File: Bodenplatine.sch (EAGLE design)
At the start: 113 parts, among them K1 RY612012, K2 RY612012, K3 RY612012, K4 RY612012, K5 RY612012, K6 RY612012, K7 RY612012, K8 RY612012, K9 RY612012, Q1 BC846BLT1SMD, Q2 BC846BLT1SMD, Q3 BC846BLT1SMD, Q4 BC846BLT1SMD, Q5 BC846BLT1SMD, Q6 BC846BLT1SMD, Q7 BC846BLT1SMD, Q8 BC846BLT1SMD, Q9 BC846BLT1SMD, X1 SPRINGCON_AST125_5X2, X10 SPRINGCON_AST125_3X2, X11 SPRINGCON_AST125_4X2, X12 SPRINGCON_AST125_4X2, X13 SPRINGCON_AST125_5X2, X14 236-403, X15 236-402, X2 SPRINGCON_AST125_5X2, X3 SPRINGCON_AST125_5X2, X4 SPRINGCON_AST125_5X2, X5 SPRINGCON_AST125_5X2, X6 SPRINGCON_AST125_5X2, X7 SPRINGCON_AST125_5X2, X8 SPRINGCON_AST125_5X2, X9 SPRINGCON_AST125_5X2

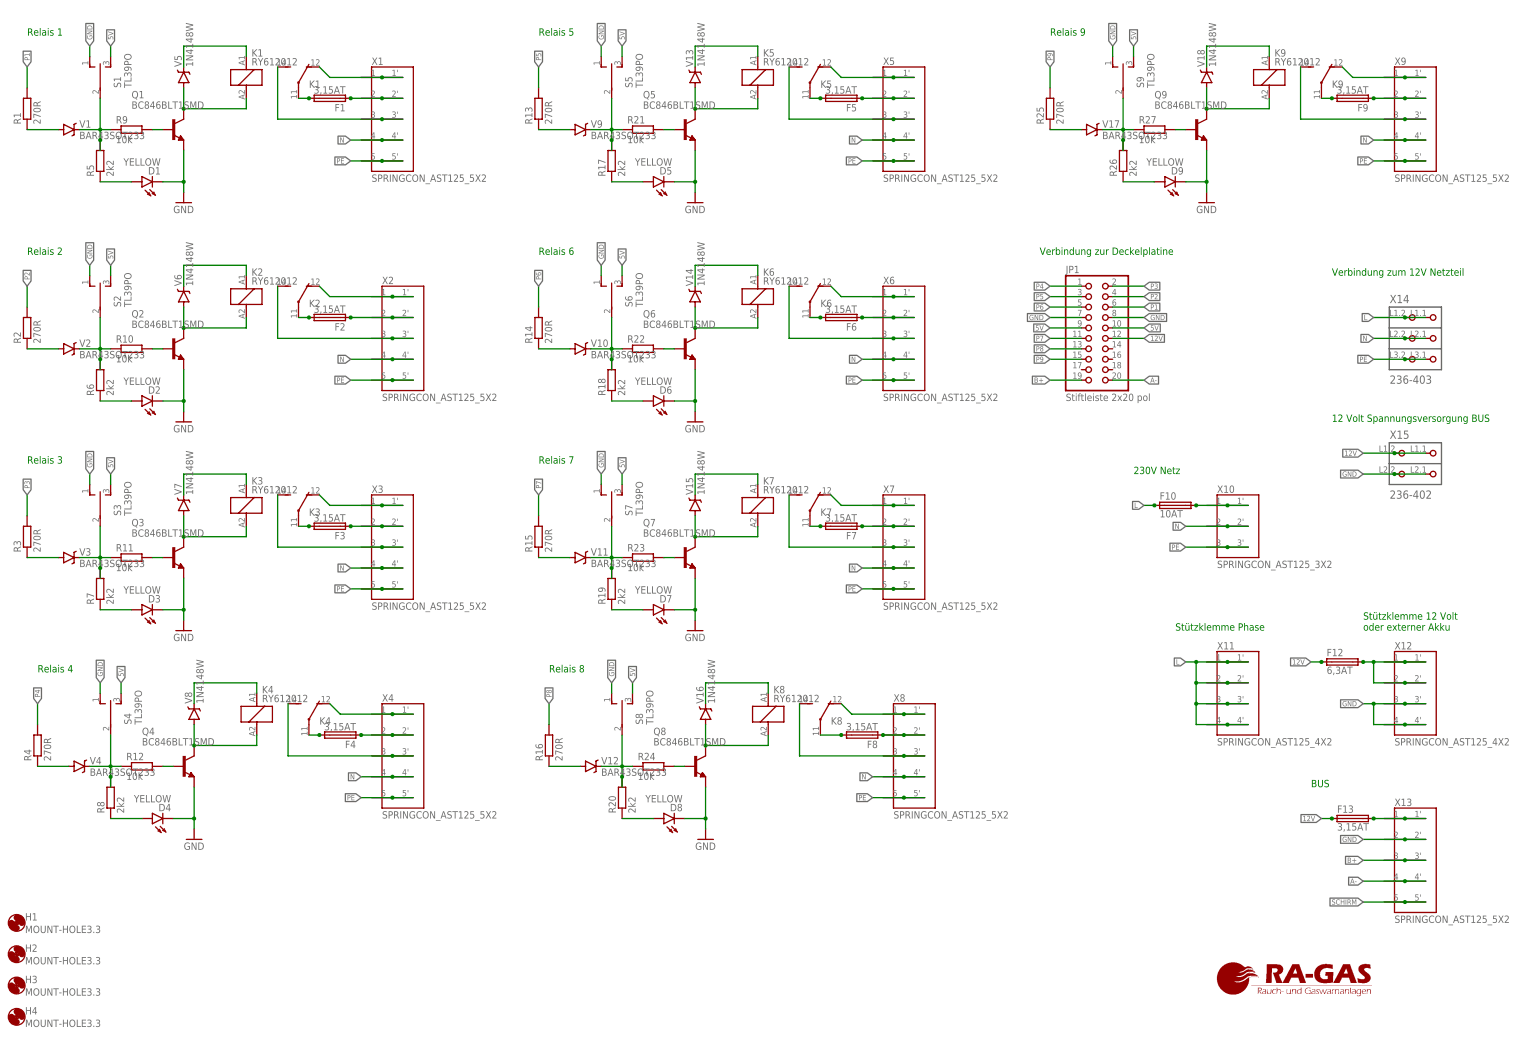
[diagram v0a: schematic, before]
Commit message: Fix 12V Spannungsversorgung vergessen ><
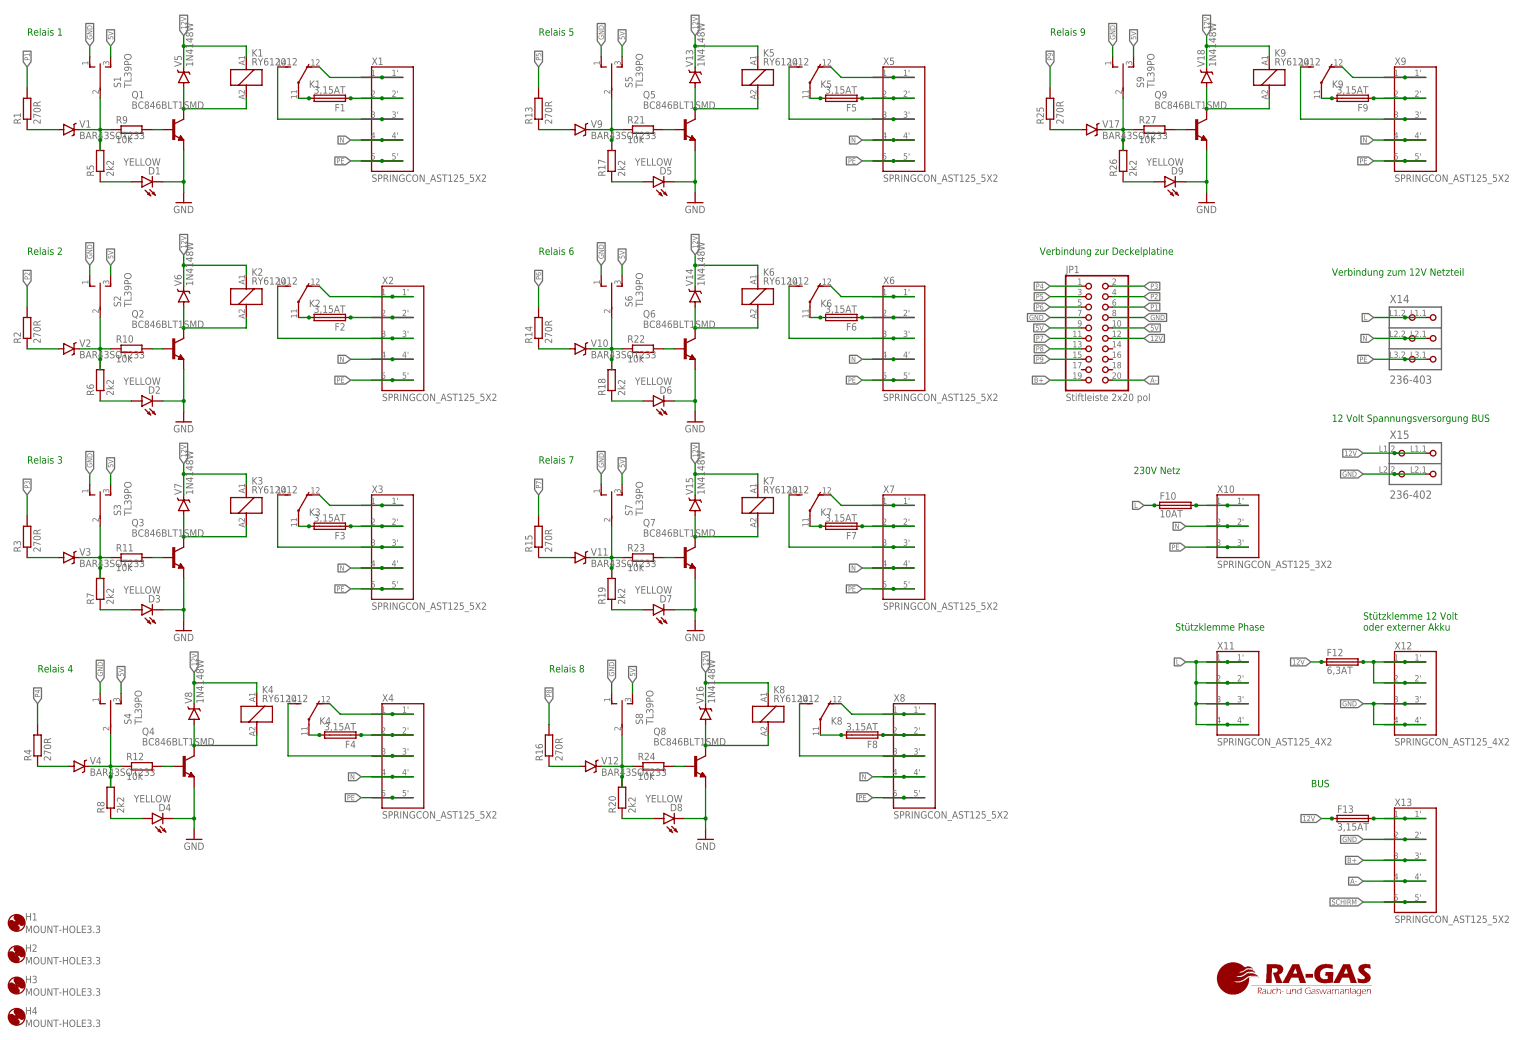
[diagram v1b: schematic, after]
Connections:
- removed net N$11: K21.1, V6.C
- removed net N$17: K31.1, V7.C
- removed net N$27: K41.1, V8.C
- removed net N$37: K51.1, V13.C
- removed net N$47: K61.1, V14.C
- removed net N$57: K71.1, V15.C
- removed net N$67: K81.1, V16.C
- removed net N$77: K91.1, V18.C
- removed net N$87: K11.1, V5.C
- net 12V: now also K11.1, K21.1, K31.1, K41.1, K51.1, K61.1, K71.1, K81.1, K91.1, V13.C, V14.C, V15.C, V16.C, V18.C, V5.C, V6.C, V7.C, V8.C
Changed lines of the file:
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@@
 <attribute name="AUTHOR" value="Stefan Müller"/>
 <attribute name="PROJEKTNAME" value="xMZ-Mod-Touch-Bodenplatine"/>
-<attribute name="VERSION" value="0.0.1"/>
+<attribute name="VERSION" value="0.9.2"/>
 </attributes>
 <variantdefs>
@@
 </segment>
 </net>
-<net name="N$11" class="0">
-<segment>
-<wire x1="50.8" y1="187.96" x2="50.8" y2="193.04" width="0.1524" layer="91"/>
-<pinref part="V6" gate="G$1" pin="C"/>
-<pinref part="K2" gate="1" pin="1"/>
-<wire x1="66.04" y1="190.5" x2="66.04" y2="193.04" width="0.1524" layer="91"/>
-<wire x1="66.04" y1="193.04" x2="50.8" y2="193.04" width="0.1524" layer="91"/>
-</segment>
-</net>
 <net name="N$5" class="0">
 <segment>
@@
 </segment>
 </net>
-<net name="N$17" class="0">
-<segment>
-<wire x1="50.8" y1="137.16" x2="50.8" y2="142.24" width="0.1524" layer="91"/>
-<wire x1="66.04" y1="142.24" x2="50.8" y2="142.24" width="0.1524" layer="91"/>
-<pinref part="V7" gate="G$1" pin="C"/>
-<pinref part="K3" gate="1" pin="1"/>
-<wire x1="66.04" y1="139.7" x2="66.04" y2="142.24" width="0.1524" layer="91"/>
-</segment>
-</net>
 <net name="N$18" class="0">
 <segment>
@@
 </segment>
 </net>
-<net name="N$27" class="0">
-<segment>
-<wire x1="53.34" y1="86.36" x2="53.34" y2="91.44" width="0.1524" layer="91"/>
-<wire x1="68.58" y1="91.44" x2="53.34" y2="91.44" width="0.1524" layer="91"/>
-<pinref part="V8" gate="G$1" pin="C"/>
-<pinref part="K4" gate="1" pin="1"/>
-<wire x1="68.58" y1="88.9" x2="68.58" y2="91.44" width="0.1524" layer="91"/>
-</segment>
-</net>
 <net name="N$28" class="0">
 <segment>
@@
 </segment>
 </net>
-<net name="N$37" class="0">
-<segment>
-<wire x1="175.26" y1="241.3" x2="175.26" y2="246.38" width="0.1524" layer="91"/>
-<wire x1="190.5" y1="246.38" x2="175.26" y2="246.38" width="0.1524" layer="91"/>
-<pinref part="V13" gate="G$1" pin="C"/>
-<pinref part="K5" gate="1" pin="1"/>
-<wire x1="190.5" y1="243.84" x2="190.5" y2="246.38" width="0.1524" layer="91"/>
-</segment>
-</net>
 <net name="N$38" class="0">
 <segment>
@@
 </segment>
 </net>
-<net name="N$47" class="0">
-<segment>
-<wire x1="175.26" y1="187.96" x2="175.26" y2="193.04" width="0.1524" layer="91"/>
-<wire x1="190.5" y1="193.04" x2="175.26" y2="193.04" width="0.1524" layer="91"/>
-<pinref part="V14" gate="G$1" pin="C"/>
-<pinref part="K6" gate="1" pin="1"/>
-<wire x1="190.5" y1="190.5" x2="190.5" y2="193.04" width="0.1524" layer="91"/>
-</segment>
-</net>
 <net name="N$48" class="0">
 <segment>
@@
 </segment>
 </net>
-<net name="N$57" class="0">
-<segment>
-<wire x1="175.26" y1="137.16" x2="175.26" y2="142.24" width="0.1524" layer="91"/>
-<wire x1="190.5" y1="142.24" x2="175.26" y2="142.24" width="0.1524" layer="91"/>
-<pinref part="V15" gate="G$1" pin="C"/>
-<pinref part="K7" gate="1" pin="1"/>
-<wire x1="190.5" y1="139.7" x2="190.5" y2="142.24" width="0.1524" layer="91"/>
-</segment>
-</net>
 <net name="N$58" class="0">
 <segment>
@@
 </segment>
 </net>
-<net name="N$67" class="0">
-<segment>
-<wire x1="177.8" y1="86.36" x2="177.8" y2="91.44" width="0.1524" layer="91"/>
-<wire x1="193.04" y1="91.44" x2="177.8" y2="91.44" width="0.1524" layer="91"/>
-<pinref part="V16" gate="G$1" pin="C"/>
-<pinref part="K8" gate="1" pin="1"/>
-<wire x1="193.04" y1="88.9" x2="193.04" y2="91.44" width="0.1524" layer="91"/>
-</segment>
-</net>
 <net name="N$68" class="0">
 <segment>
@@
 </segment>
 </net>
-<net name="N$77" class="0">
-<segment>
-<wire x1="299.72" y1="241.3" x2="299.72" y2="246.38" width="0.1524" layer="91"/>
-<wire x1="314.96" y1="246.38" x2="299.72" y2="246.38" width="0.1524" layer="91"/>
-<pinref part="V18" gate="G$1" pin="C"/>
-<pinref part="K9" gate="1" pin="1"/>
-<wire x1="314.96" y1="243.84" x2="314.96" y2="246.38" width="0.1524" layer="91"/>
-</segment>
-</net>
 <net name="N$78" class="0">
 <segment>
@@
 </segment>
 </net>
-<net name="N$87" class="0">
-<segment>
-<wire x1="50.8" y1="241.3" x2="50.8" y2="246.38" width="0.1524" layer="91"/>
-<pinref part="V5" gate="G$1" pin="C"/>
-<pinref part="K1" gate="1" pin="1"/>
-<wire x1="66.04" y1="243.84" x2="66.04" y2="246.38" width="0.1524" layer="91"/>
-<wire x1="66.04" y1="246.38" x2="50.8" y2="246.38" width="0.1524" layer="91"/>
-</segment>
-</net>
 <net name="N$88" class="0">
 <segment>
@@
 <junction x="345.44" y="147.32"/>
 </segment>
-</net>
+<segment>
+<wire x1="299.72" y1="241.3" x2="299.72" y2="246.38" width="0.1524" layer="91"/>
+<wire x1="314.96" y1="246.38" x2="299.72" y2="246.38" width="0.1524" layer="91"/>
+<pinref part="V18" gate="G$1" pin="C"/>
+<pinref part="K9" gate="1" pin="1"/>
+<wire x1="314.96" y1="243.84" x2="314.96" y2="246.38" width="0.1524" layer="91"/>
+<wire x1="299.72" y1="246.38" x2="299.72" y2="248.92" width="0.1524" layer="91"/>
+<junction x="299.72" y="246.38"/>
+<label x="299.72" y="248.92" size="1.27" layer="95" rot="R90" xref="yes"/>
+</segment>
+<segment>
+<wire x1="175.26" y1="241.3" x2="175.26" y2="246.38" width="0.1524" layer="91"/>
+<wire x1="190.5" y1="246.38" x2="175.26" y2="246.38" width="0.1524" layer="91"/>
+<pinref part="V13" gate="G$1" pin="C"/>
+<pinref part="K5" gate="1" pin="1"/>
+<wire x1="190.5" y1="243.84" x2="190.5" y2="246.38" width="0.1524" layer="91"/>
+<wire x1="175.26" y1="246.38" x2="175.26" y2="248.92" width="0.1524" layer="91"/>
+<junction x="175.26" y="246.38"/>
+<label x="175.26" y="248.92" size="1.27" layer="95" rot="R90" xref="yes"/>
+</segment>
+<segment>
+<wire x1="175.26" y1="187.96" x2="175.26" y2="193.04" width="0.1524" layer="91"/>
+<wire x1="190.5" y1="193.04" x2="175.26" y2="193.04" width="0.1524" layer="91"/>
+<pinref part="V14" gate="G$1" pin="C"/>
+<pinref part="K6" gate="1" pin="1"/>
+<wire x1="190.5" y1="190.5" x2="190.5" y2="193.04" width="0.1524" layer="91"/>
+<wire x1="175.26" y1="193.04" x2="175.26" y2="195.58" width="0.1524" layer="91"/>
+<junction x="175.26" y="193.04"/>
+<label x="175.26" y="195.58" size="1.27" layer="95" rot="R90" xref="yes"/>
+</segment>
+<segment>
+<wire x1="175.26" y1="137.16" x2="175.26" y2="142.24" width="0.1524" layer="91"/>
+<wire x1="190.5" y1="142.24" x2="175.26" y2="142.24" width="0.1524" layer="91"/>
+<pinref part="V15" gate="G$1" pin="C"/>
+<pinref part="K7" gate="1" pin="1"/>
+<wire x1="190.5" y1="139.7" x2="190.5" y2="142.24" width="0.1524" layer="91"/>
+<wire x1="175.26" y1="142.24" x2="175.26" y2="144.78" width="0.1524" layer="91"/>
+<junction x="175.26" y="142.24"/>
+<label x="175.26" y="144.78" size="1.27" layer="95" rot="R90" xref="yes"/>
+</segment>
+<segment>
+<wire x1="177.8" y1="86.36" x2="177.8" y2="91.44" width="0.1524" layer="91"/>
+<wire x1="193.04" y1="91.44" x2="177.8" y2="91.44" width="0.1524" layer="91"/>
+<pinref part="V16" gate="G$1" pin="C"/>
+<pinref part="K8" gate="1" pin="1"/>
+<wire x1="193.04" y1="88.9" x2="193.04" y2="91.44" width="0.1524" layer="91"/>
+<wire x1="177.8" y1="91.44" x2="177.8" y2="93.98" width="0.1524" layer="91"/>
+<junction x="177.8" y="91.44"/>
+<label x="177.8" y="93.98" size="1.27" layer="95" rot="R90" xref="yes"/>
+</segment>
+<segment>
+<wire x1="53.34" y1="86.36" x2="53.34" y2="91.44" width="0.1524" layer="91"/>
+<wire x1="68.58" y1="91.44" x2="53.34" y2="91.44" width="0.1524" layer="91"/>
+<pinref part="V8" gate="G$1" pin="C"/>
+<pinref part="K4" gate="1" pin="1"/>
+<wire x1="68.58" y1="88.9" x2="68.58" y2="91.44" width="0.1524" layer="91"/>
+<wire x1="53.34" y1="91.44" x2="53.34" y2="93.98" width="0.1524" layer="91"/>
+<junction x="53.34" y="91.44"/>
+<label x="53.34" y="93.98" size="1.27" layer="95" rot="R90" xref="yes"/>
+</segment>
+<segment>
+<wire x1="50.8" y1="137.16" x2="50.8" y2="142.24" width="0.1524" layer="91"/>
+<wire x1="66.04" y1="142.24" x2="50.8" y2="142.24" width="0.1524" layer="91"/>
+<pinref part="V7" gate="G$1" pin="C"/>
+<pinref part="K3" gate="1" pin="1"/>
+<wire x1="66.04" y1="139.7" x2="66.04" y2="142.24" width="0.1524" layer="91"/>
+<wire x1="50.8" y1="142.24" x2="50.8" y2="144.78" width="0.1524" layer="91"/>
+<junction x="50.8" y="142.24"/>
+<label x="50.8" y="144.78" size="1.27" layer="95" rot="R90" xref="yes"/>
+</segment>
+<segment>
+<wire x1="50.8" y1="187.96" x2="50.8" y2="193.04" width="0.1524" layer="91"/>
+<pinref part="V6" gate="G$1" pin="C"/>
+<pinref part="K2" gate="1" pin="1"/>
+<wire x1="66.04" y1="190.5" x2="66.04" y2="193.04" width="0.1524" layer="91"/>
+<wire x1="66.04" y1="193.04" x2="50.8" y2="193.04" width="0.1524" layer="91"/>
+<wire x1="50.8" y1="193.04" x2="50.8" y2="195.58" width="0.1524" layer="91"/>
+<junction x="50.8" y="193.04"/>
+<label x="50.8" y="195.58" size="1.27" layer="95" rot="R90" xref="yes"/>
+</segment>
+<segment>
+<wire x1="50.8" y1="241.3" x2="50.8" y2="246.38" width="0.1524" layer="91"/>
+<pinref part="V5" gate="G$1" pin="C"/>
+<pinref part="K1" gate="1" pin="1"/>
+<wire x1="66.04" y1="243.84" x2="66.04" y2="246.38" width="0.1524" layer="91"/>
+<wire x1="66.04" y1="246.38" x2="50.8" y2="246.38" width="0.1524" layer="91"/>
+<wire x1="50.8" y1="246.38" x2="50.8" y2="248.92" width="0.1524" layer="91"/>
+<junction x="50.8" y="246.38"/>
+<label x="50.8" y="248.92" size="1.27" layer="95" rot="R90" xref="yes"/>
+</segment>
+</net>
